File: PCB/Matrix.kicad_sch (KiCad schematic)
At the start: 49 parts, among them SW1 CPG151101S11, SW10 CPG151101S11, SW11 CPG151101S11, SW12 CPG151101S11, SW13 CPG151101S11, SW14 CPG151101S11, SW15 CPG151101S11, SW16 CPG151101S11, SW17 CPG151101S11, SW18 CPG151101S11, SW19 CPG151101S11, SW2 CPG151101S11, SW20 CPG151101S11, SW21 CPG151101S11, SW22 CPG151101S11, SW23 CPG151101S11, SW24 CPG151101S11, SW25 CPG151101S11, SW26 CPG151101S11, SW27 CPG151101S11, SW28 CPG151101S11, SW29 CPG151101S11, SW3 CPG151101S11, SW30 CPG151101S11, SW31 CPG151101S11, SW4 CPG151101S11, SW5 CPG151101S11, SW6 CPG151101S11, SW7 CPG151101S11, SW8 CPG151101S11, SW9 CPG151101S11, U6 74HC595

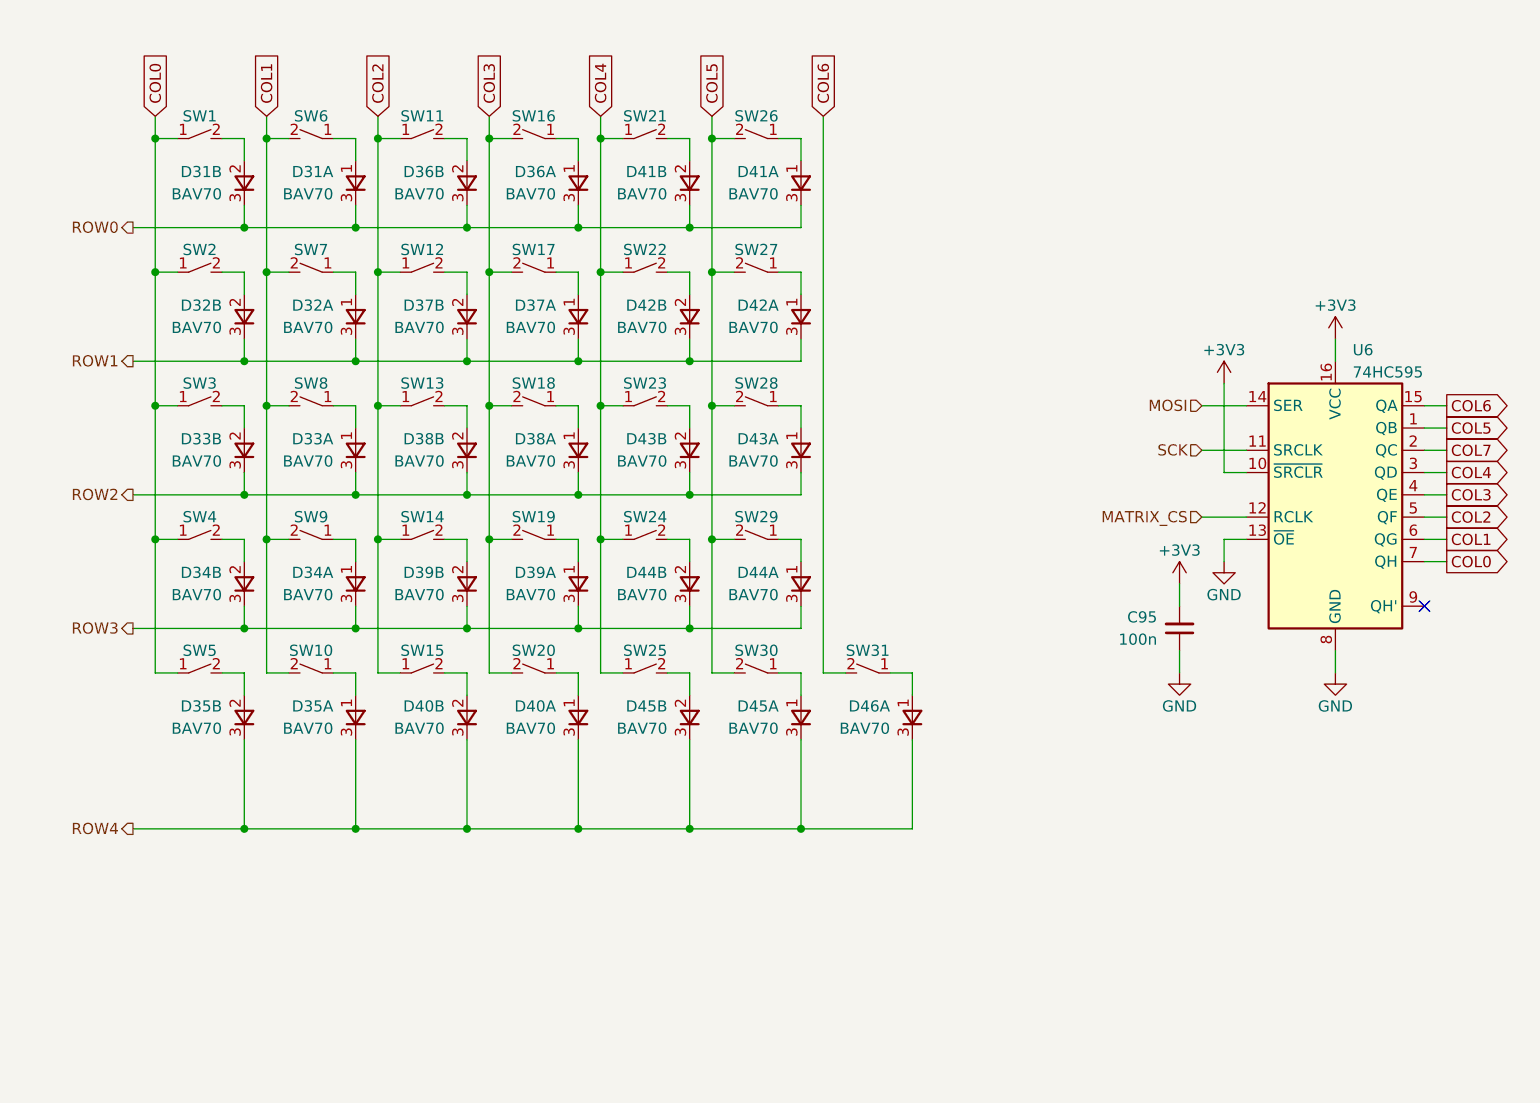
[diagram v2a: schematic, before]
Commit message: 23/08/2023 update
Changed MCU to nRF52840. Added nPM1300 PMIC for power management. Replaced SSD1351 display with Nice!View. Added Kailh Choc V1/V2 and Gateron KS-27/KS-33 support.
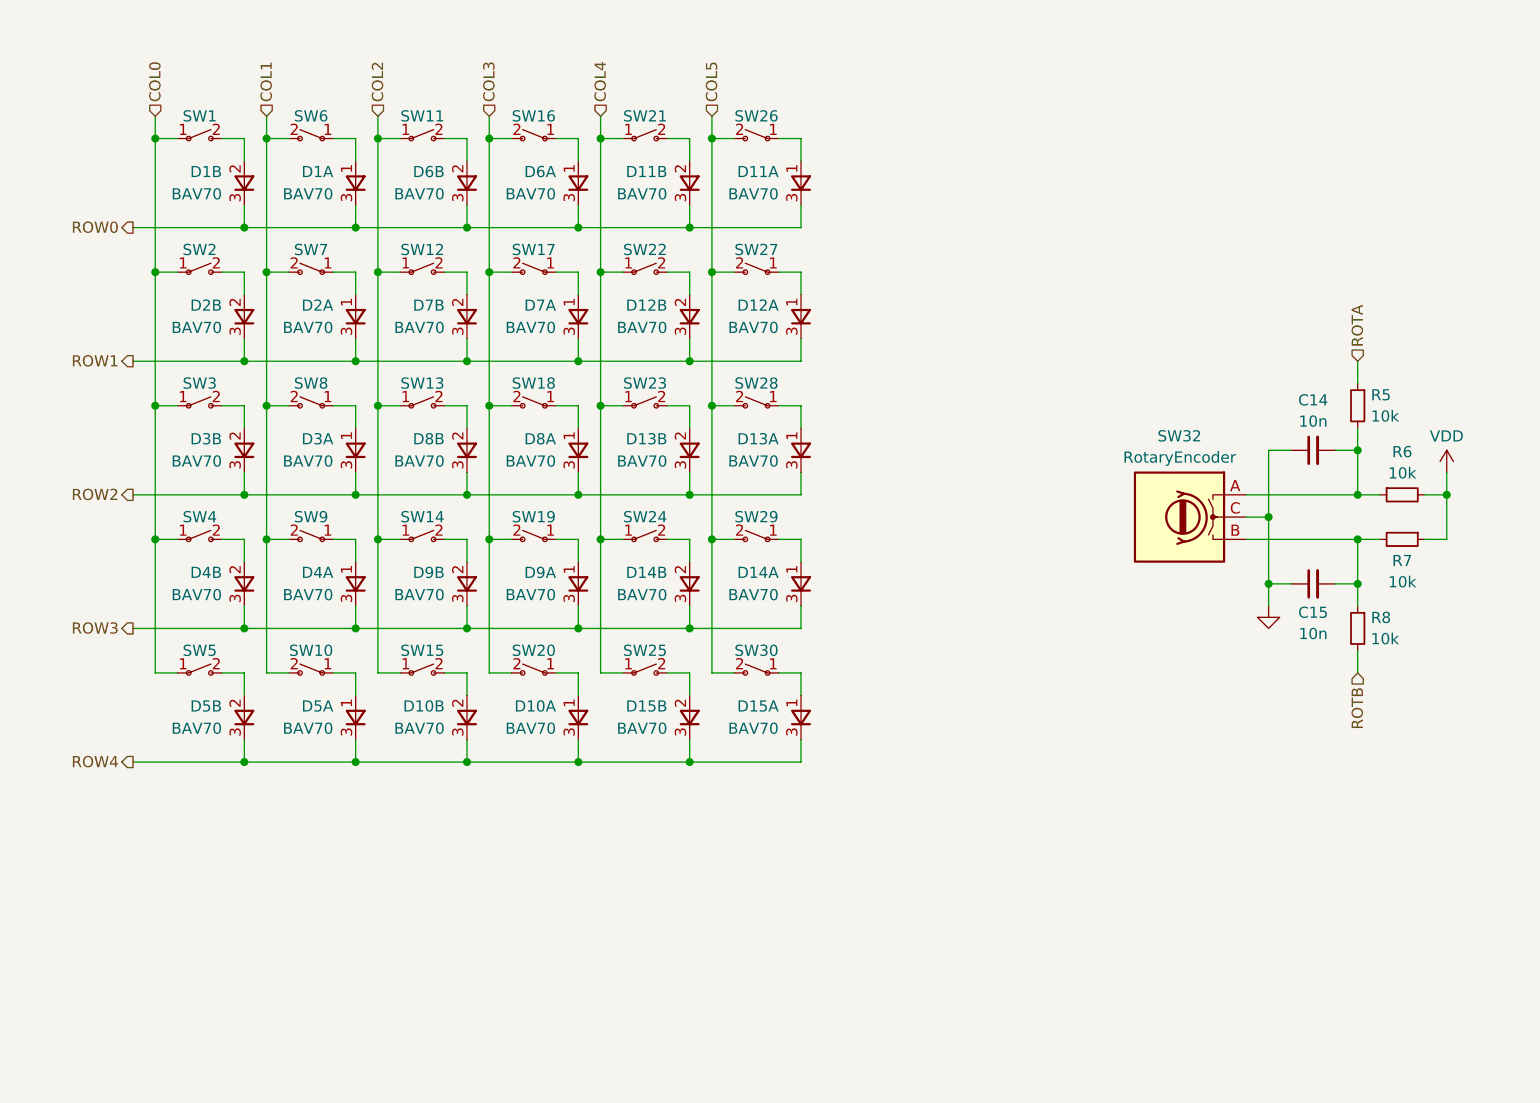
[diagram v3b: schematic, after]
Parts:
- removed C95: 100n, Capacitor_SMD:C_0402_1005Metric, symbol Device:C_Small
- removed D46: BAV70, Cantaloupe:SOT-23-3, symbol Honeydew:D_Dual_CommonCathode_AAK_Split_Small
- removed SW31: CPG151101S11, Cantaloupe:MXOnly-1U-Hotswap-Flippable, symbol Cantaloupe:SW_SPST_Small
- removed U6: 74HC595, Cantaloupe:SOIC-16_3.9x9.9mm_P1.27mm, symbol 74xx:74HC595
- added C14, C15: 10n, Ariamelon-Device:C_0402_1005Metric, symbol Device:C_Small
- added R5, R6, R7, R8: 10k, Ariamelon-Device:R_0402_1005Metric, symbol Device:R_Small
- added SW32: RotaryEncoder, Cantaloupe:EVQVVD00203B-Flippable, symbol Device:RotaryEncoder
- D1: renamed from D31; footprint Cantaloupe:SOT-23-3 -> Ariamelon-Package:SOT-23-3; symbol Honeydew:D_Dual_CommonCathode_AAK_Split_Small -> Ariamelon-Device:D_Dual_CommonCathode_AAK_Split_Small
- D10: renamed from D40; footprint Cantaloupe:SOT-23-3 -> Ariamelon-Package:SOT-23-3; symbol Honeydew:D_Dual_CommonCathode_AAK_Split_Small -> Ariamelon-Device:D_Dual_CommonCathode_AAK_Split_Small
- D11: renamed from D41; footprint Cantaloupe:SOT-23-3 -> Ariamelon-Package:SOT-23-3; symbol Honeydew:D_Dual_CommonCathode_AAK_Split_Small -> Ariamelon-Device:D_Dual_CommonCathode_AAK_Split_Small
- D12: renamed from D42; footprint Cantaloupe:SOT-23-3 -> Ariamelon-Package:SOT-23-3; symbol Honeydew:D_Dual_CommonCathode_AAK_Split_Small -> Ariamelon-Device:D_Dual_CommonCathode_AAK_Split_Small
- D13: renamed from D43; footprint Cantaloupe:SOT-23-3 -> Ariamelon-Package:SOT-23-3; symbol Honeydew:D_Dual_CommonCathode_AAK_Split_Small -> Ariamelon-Device:D_Dual_CommonCathode_AAK_Split_Small
- D14: renamed from D44; footprint Cantaloupe:SOT-23-3 -> Ariamelon-Package:SOT-23-3; symbol Honeydew:D_Dual_CommonCathode_AAK_Split_Small -> Ariamelon-Device:D_Dual_CommonCathode_AAK_Split_Small
- D15: renamed from D45; footprint Cantaloupe:SOT-23-3 -> Ariamelon-Package:SOT-23-3; symbol Honeydew:D_Dual_CommonCathode_AAK_Split_Small -> Ariamelon-Device:D_Dual_CommonCathode_AAK_Split_Small
- D2: renamed from D32; footprint Cantaloupe:SOT-23-3 -> Ariamelon-Package:SOT-23-3; symbol Honeydew:D_Dual_CommonCathode_AAK_Split_Small -> Ariamelon-Device:D_Dual_CommonCathode_AAK_Split_Small
- D3: renamed from D33; footprint Cantaloupe:SOT-23-3 -> Ariamelon-Package:SOT-23-3; symbol Honeydew:D_Dual_CommonCathode_AAK_Split_Small -> Ariamelon-Device:D_Dual_CommonCathode_AAK_Split_Small
- D4: renamed from D34; footprint Cantaloupe:SOT-23-3 -> Ariamelon-Package:SOT-23-3; symbol Honeydew:D_Dual_CommonCathode_AAK_Split_Small -> Ariamelon-Device:D_Dual_CommonCathode_AAK_Split_Small
- D5: renamed from D35; footprint Cantaloupe:SOT-23-3 -> Ariamelon-Package:SOT-23-3; symbol Honeydew:D_Dual_CommonCathode_AAK_Split_Small -> Ariamelon-Device:D_Dual_CommonCathode_AAK_Split_Small
- D6: renamed from D36; footprint Cantaloupe:SOT-23-3 -> Ariamelon-Package:SOT-23-3; symbol Honeydew:D_Dual_CommonCathode_AAK_Split_Small -> Ariamelon-Device:D_Dual_CommonCathode_AAK_Split_Small
- D7: renamed from D37; footprint Cantaloupe:SOT-23-3 -> Ariamelon-Package:SOT-23-3; symbol Honeydew:D_Dual_CommonCathode_AAK_Split_Small -> Ariamelon-Device:D_Dual_CommonCathode_AAK_Split_Small
- D8: renamed from D38; footprint Cantaloupe:SOT-23-3 -> Ariamelon-Package:SOT-23-3; symbol Honeydew:D_Dual_CommonCathode_AAK_Split_Small -> Ariamelon-Device:D_Dual_CommonCathode_AAK_Split_Small
- D9: renamed from D39; footprint Cantaloupe:SOT-23-3 -> Ariamelon-Package:SOT-23-3; symbol Honeydew:D_Dual_CommonCathode_AAK_Split_Small -> Ariamelon-Device:D_Dual_CommonCathode_AAK_Split_Small
- SW1, SW10, SW11, SW12, SW13, SW14, SW15, SW16, SW17, SW18, SW19, SW2, SW20, SW21, SW22, SW23, SW24, SW25, SW26, SW27, SW28, SW29, SW3, SW30, SW4, SW5, SW6, SW7, SW8, SW9: footprint Cantaloupe:MXOnly-1U-Hotswap-Flippable -> Ariamelon-Switch:SW_MX-Choc-KS27_1U_Hotswap_Flippable; symbol Cantaloupe:SW_SPST_Small -> Ariamelon-Switch:SW_SPST_Small
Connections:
- net GND: now also C14.1, C15.1, SW32.C
- new net: C14.2, R5.2, R6.1, SW32.A
- new net: C15.2, R7.2, R8.1, SW32.B
- new net ROTA: R5.1
- new net ROTB: R8.2
- new net VDD: R6.2, R7.1
- no-connect marks 1 -> 0

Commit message: 24/08/2023 update
Finished routing. Consolidated all libraries into Ariamelon's Kicad Master Library. Added PCM12 switch connected to nPM1300 GPIO. Rearranged components and rerouted.
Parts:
- SW32: footprint Cantaloupe:EVQVVD00203B-Flippable -> Ariamelon-RotaryEncoder:RotaryEncoder_Panasonic_EVQVVD00203B-Flippable
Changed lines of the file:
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@@
       (effects (font (size 1.27 1.27)))
     )
-    (property "Footprint" "Cantaloupe:EVQVVD00203B-Flippable" (at 148.59 64.516 0)
+    (property "Footprint" "Ariamelon-RotaryEncoder:RotaryEncoder_Panasonic_EVQVVD00203B-Flippable" (at 148.59 64.516 0)
       (effects (font (size 1.27 1.27)) hide)
     )

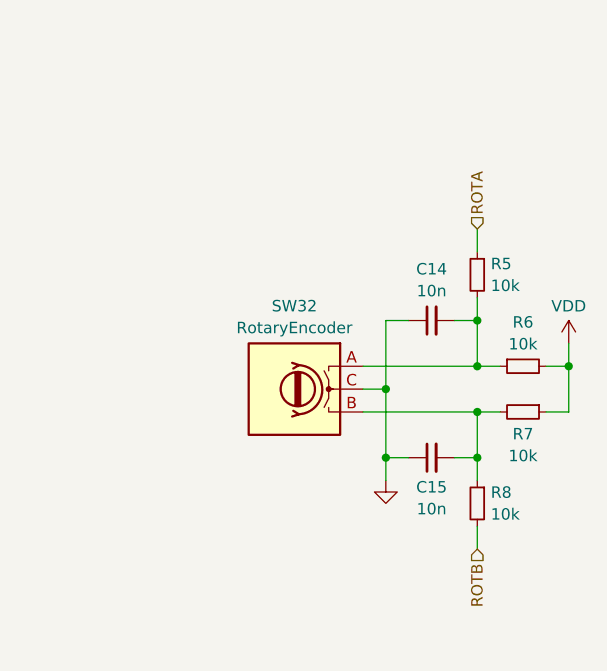
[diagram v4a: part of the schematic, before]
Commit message: Cantaloupe V3.0 name changed to CantaloupeBT V1.0 ('BT-V1' branch). Key features updated. Design will be reworked in the coming days!
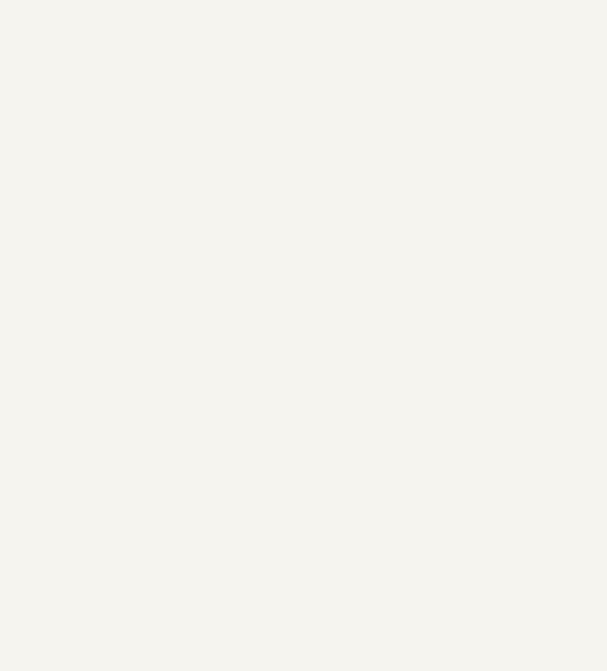
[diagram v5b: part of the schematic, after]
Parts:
- removed C14, C15: 10n, Ariamelon-Device:C_0402_1005Metric, symbol Device:C_Small
- removed R5, R6, R7, R8: 10k, Ariamelon-Device:R_0402_1005Metric, symbol Device:R_Small
- removed SW32: RotaryEncoder, Ariamelon-RotaryEncoder:RotaryEncoder_Panasonic_EVQVVD00203B-Flippable, symbol Device:RotaryEncoder
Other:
- title: Cantaloupe split ergonomic keyboard -> CantaloupeLP split ergonomic keyboard
